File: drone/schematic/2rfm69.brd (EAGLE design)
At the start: 160 x 100 mm, 13 parts, among them IC1 MEGA8-P, Q1 16MHz, U1 RFM692, U2 RFM692

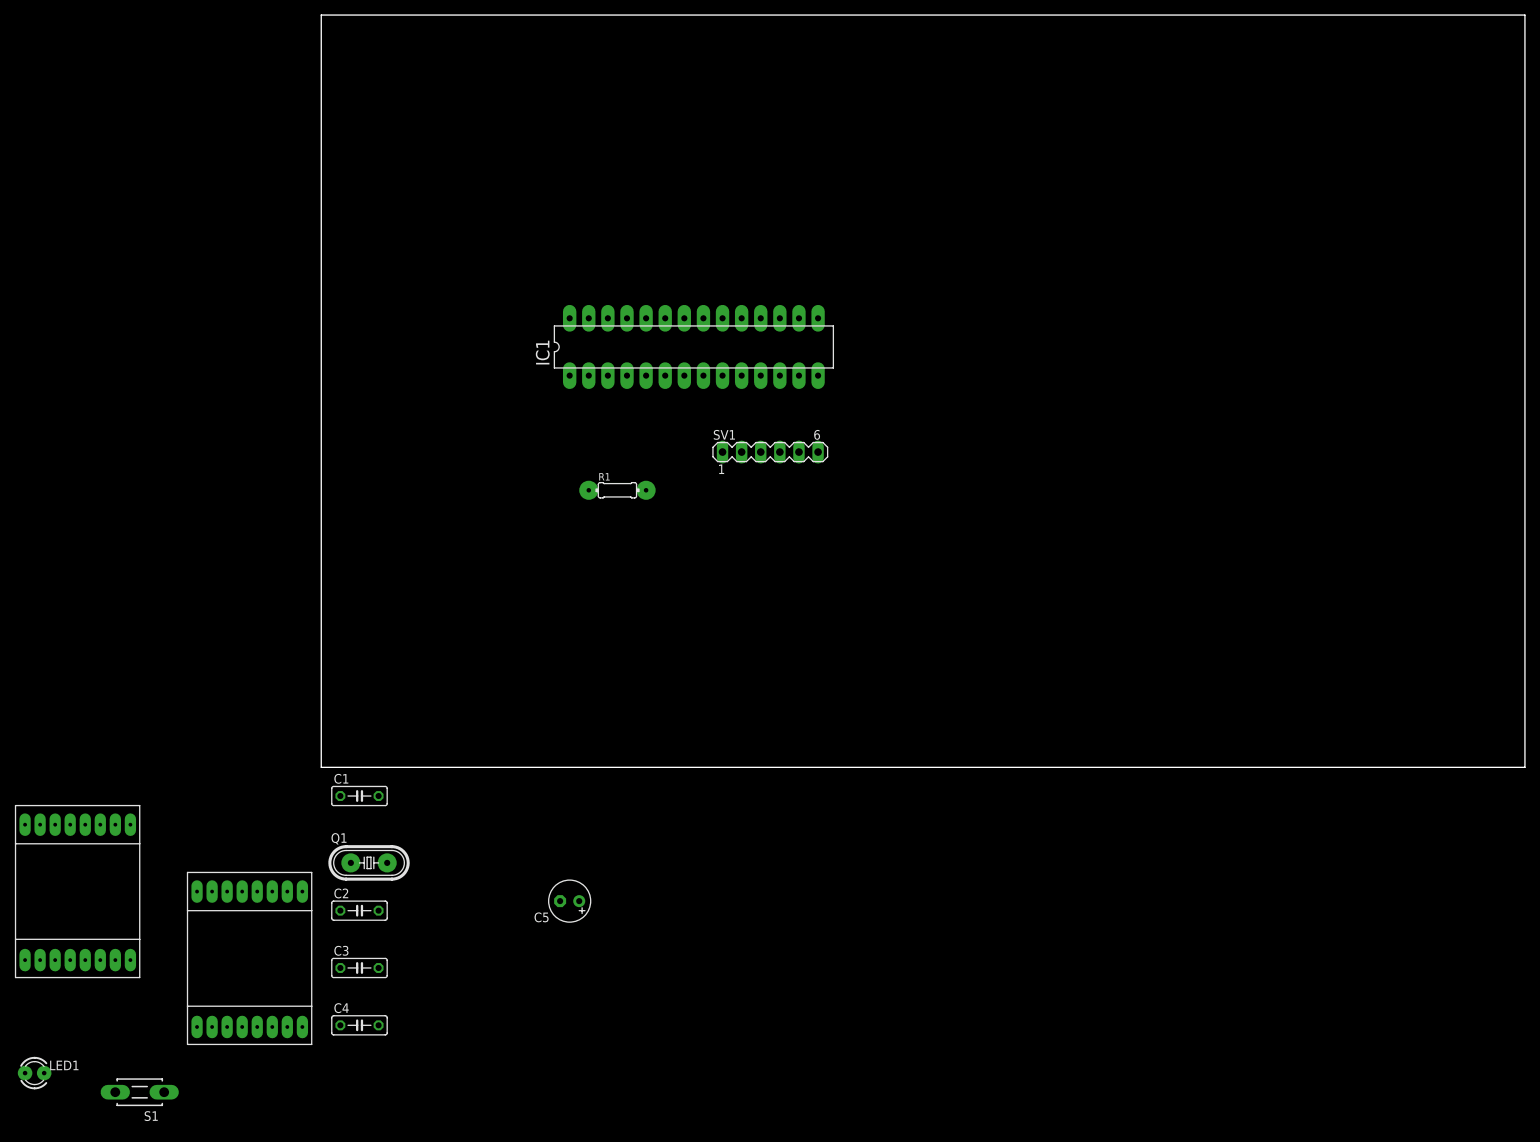
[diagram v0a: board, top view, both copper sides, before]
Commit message: schematic drone
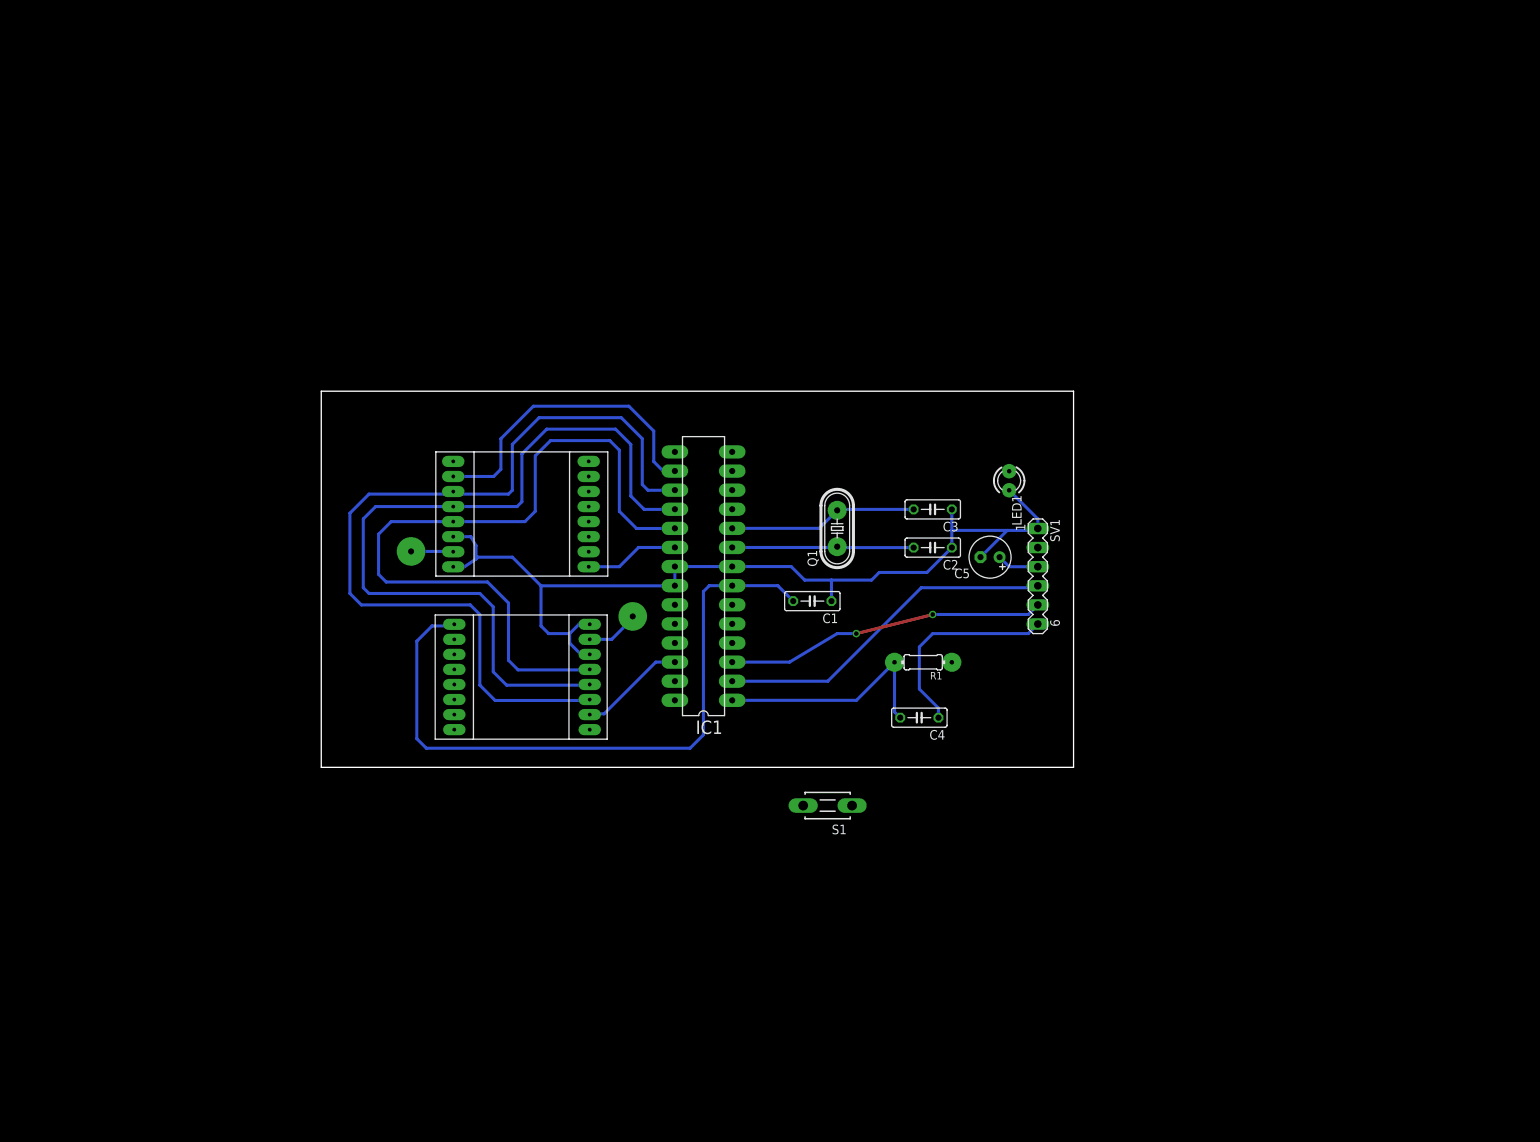
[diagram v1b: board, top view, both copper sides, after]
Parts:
- added U$1, U$2: ANT, rfm69:ANT
- moved LED1 151.6 mm to (91.4, 38.1), turned to 270 degrees
- moved S1 99.1 mm to (67.3, -5.08)
- moved C3 97.6 mm to (81.3, 34.3), turned to 180 degrees
- moved C2 90.2 mm to (81.3, 29.2), turned to 180 degrees
- moved C4 84.9 mm to (79.5, 6.60), turned to 180 degrees
- moved U2 78.4 mm to (26.7, 34.3), turned to 270 degrees
- moved Q1 76.5 mm to (68.6, 31.8), turned to 90 degrees
- moved C5 72.2 mm to (88.9, 27.9)
- moved C1 65.5 mm to (65.3, 22.1), turned to 180 degrees
- moved U1 52.0 mm to (26.6, 11.4), turned to 90 degrees
- moved R1 46.6 mm to (80.0, 14.0), turned to 180 degrees
- moved SV1 39.2 mm to (95.2, 25.4), turned to 270 degrees
- moved IC1 30.5 mm to (50.8, 25.4), turned to 90 degrees
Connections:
- new net D10_SS2: IC1.16, U2.15
- new net D11_MOSI: IC1.17, U1.14, U2.14
- new net D12_MISO: IC1.18, U1.13, U2.13
- new net D13_SCK: IC1.19, U1.12, U2.12
- new net D2_INT2: IC1.4, U2.2
- new net D3_INT1: IC1.5, U1.2
- new net D8: IC1.14
- new net D9: IC1.15
- new net N$4: U$2.ANT, U1.10
- new net N$5: U$1.ANT, U2.10
- new net SS1: IC1.26, U1.15
- net +3V3: now also U1.8
- net GND: now also U1.11, U1.9
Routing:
- net GND: track 0.00 -> 127.3 mm
- net D11_MOSI: track 0.00 -> 114.3 mm
- net +3V3: track 0.00 -> 108.5 mm
- net D12_MISO: track 0.00 -> 108.3 mm
- net D13_SCK: track 0.00 -> 101.6 mm
- net D0_RX: track 0.00 -> 45.9 mm
- net D1_TX: track 0.00 -> 42.5 mm, vias 0 -> 2
- net D10_SS2: track 0.00 -> 41.7 mm
- net RST: track 0.00 -> 31.4 mm
- net N$3: track 0.00 -> 27.5 mm
- net N$2: track 0.00 -> 25.2 mm
- net N$1: track 0.00 -> 24.2 mm
- net SS1: track 0.00 -> 14.2 mm
- net N$4: track 0.00 -> 7.13 mm
- net N$5: track 0.00 -> 5.62 mm
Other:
- board size 160 x 100 mm -> 100 x 50 mm

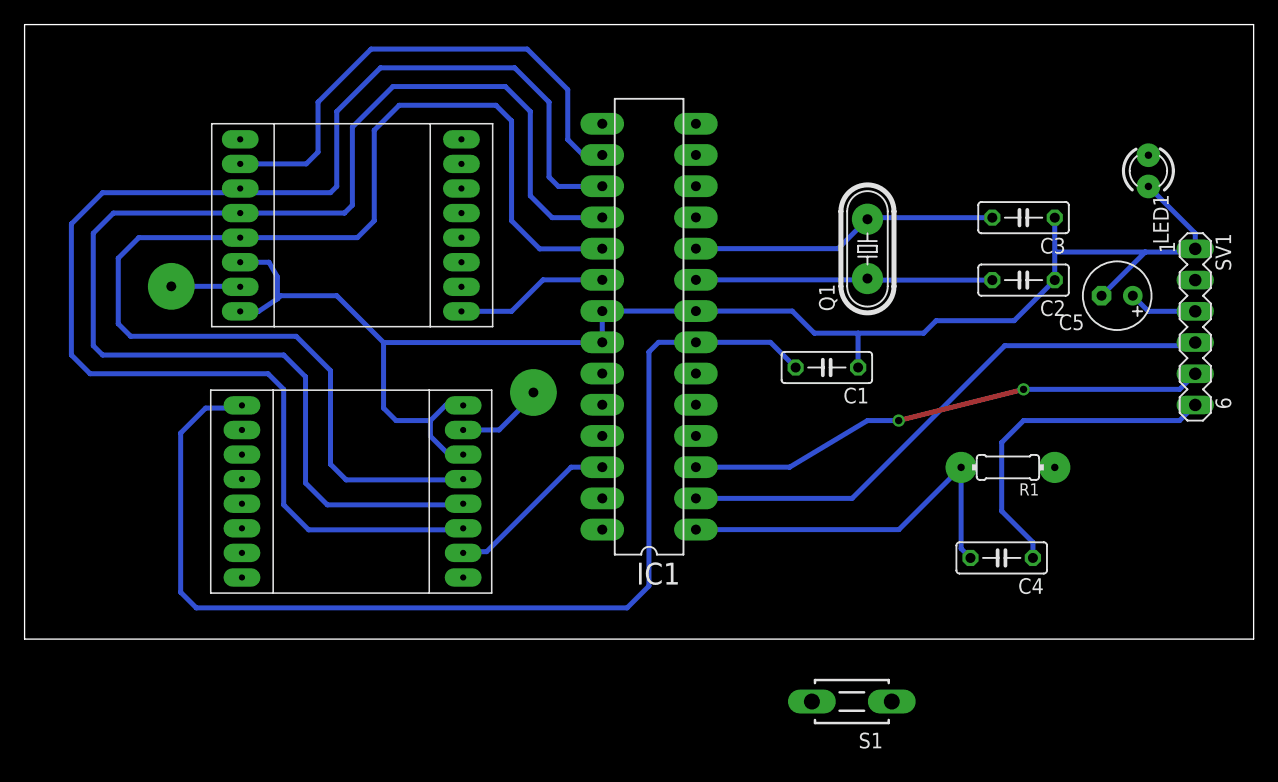
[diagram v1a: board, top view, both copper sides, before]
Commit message: test drone DIP schematic complete
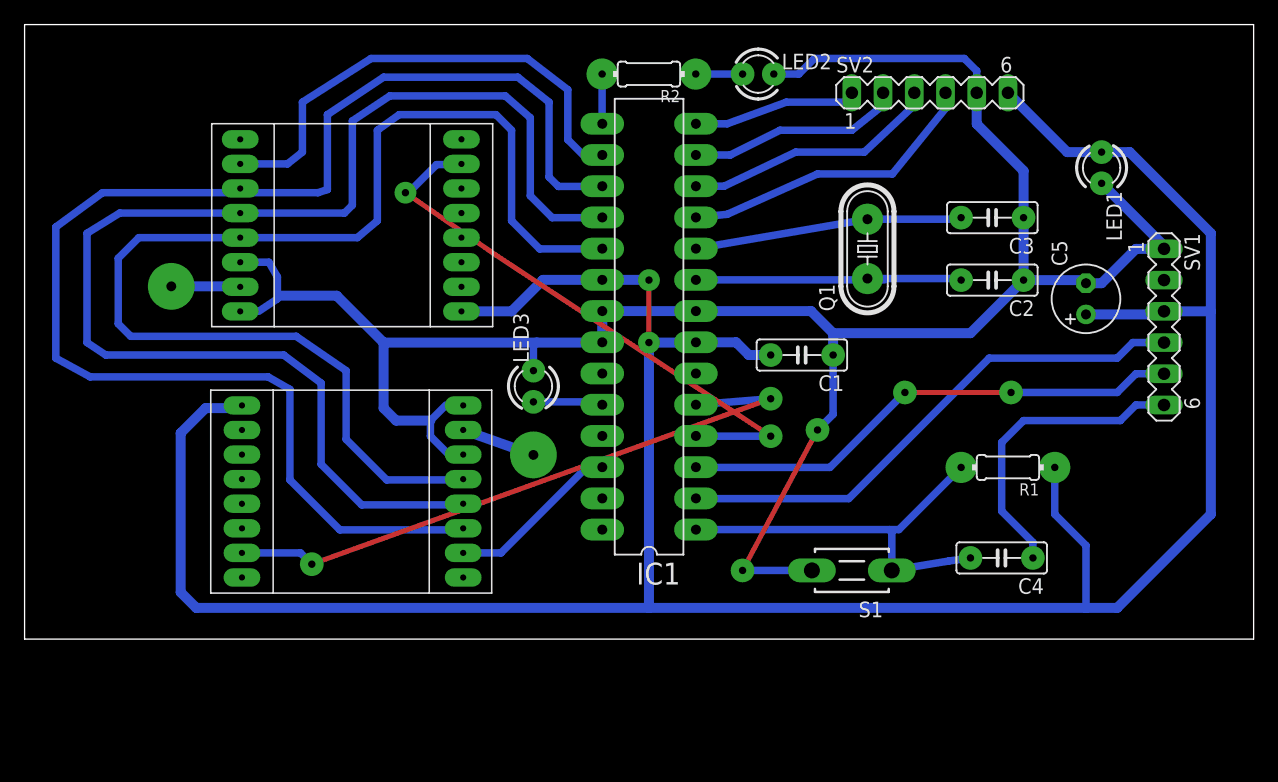
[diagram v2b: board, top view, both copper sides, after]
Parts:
- added LED2, LED3: (no value), led:LED3MM
- added R2: 1k, rcl:0204/7
- added SV2: (no value), con-lstb:MA06-1
- moved S1 10.7 mm to (67.3, 5.59)
- moved U$2 5.08 mm to (41.4, 15.0)
- moved LED1 3.82 mm to (87.6, 38.4)
- moved C5 2.55 mm to (86.4, 27.7), turned to 90 degrees
- moved C2 2.54 mm to (78.7, 29.2)
- moved C3 2.54 mm to (78.7, 34.3)
- moved SV1 2.54 mm to (92.7, 25.4)
- moved C1 2.27 mm to (63.2, 23.1)
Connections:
- new net D5: IC1.11, SV2.4
- new net D6: IC1.12, SV2.3
- new net D7: IC1.13, SV2.2
- new net N$6: LED2.A, R2.1
- new net N$7: IC1.24, LED3.A
- net +3V3: now also SV2.6
- net D8: now also SV2.1
- net D9: now also R2.2
- net GND: now also LED2.K, LED3.K, SV2.5
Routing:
- net +3V3: track 108.5 -> 226.9 mm, vias 0 -> 2
- net GND: track 127.3 -> 179.2 mm, vias 0 -> 2
- net D3_INT1: track 0.00 -> 51.9 mm, vias 0 -> 2
- net D2_INT2: track 0.00 -> 47.3 mm, vias 0 -> 2
- net D5: track 0.00 -> 24.8 mm
- net D6: track 0.00 -> 20.9 mm
- net D7: track 0.00 -> 17.4 mm
- net D8: track 0.00 -> 14.0 mm
- net N$7: track 0.00 -> 5.70 mm
- net D9: track 0.00 -> 5.06 mm
- net N$6: track 0.00 -> 3.81 mm
- net N$2: track 25.2 -> 21.8 mm
- net D13_SCK: track 101.6 -> 98.9 mm
- net N$3: track 27.5 -> 24.9 mm
- net D0_RX: track 45.9 -> 43.4 mm
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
